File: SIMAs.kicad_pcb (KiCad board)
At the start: 2 copper layers, 67.5 x 75.5 mm, 89 parts, among them J1 USB_C_Receptacle_PowerOnly_6P, J10 Conn_01x02_Pin, J11 Conn_01x03_Pin, J12 Conn_01x03_Pin, J13 Conn_01x05_Pin, J14 Conn_01x02_Pin, J2 Conn_01x02_Socket, J3 Conn_01x04_Socket, J4 Conn_01x04_Socket, J5 Conn_01x04_Socket, J6 Conn_01x03_Socket, J7 Bateria, J8 Conn_01x02_Socket, J9 Conn_01x03_Socket, Q1 QM6015D, U1 mini_esp32, U2 BQ25628ERYKR, U3 TPS611781RNWR, U4 TLV61070ADBV, U8 DRV8876PWPR, U9 DRV8876PWPR

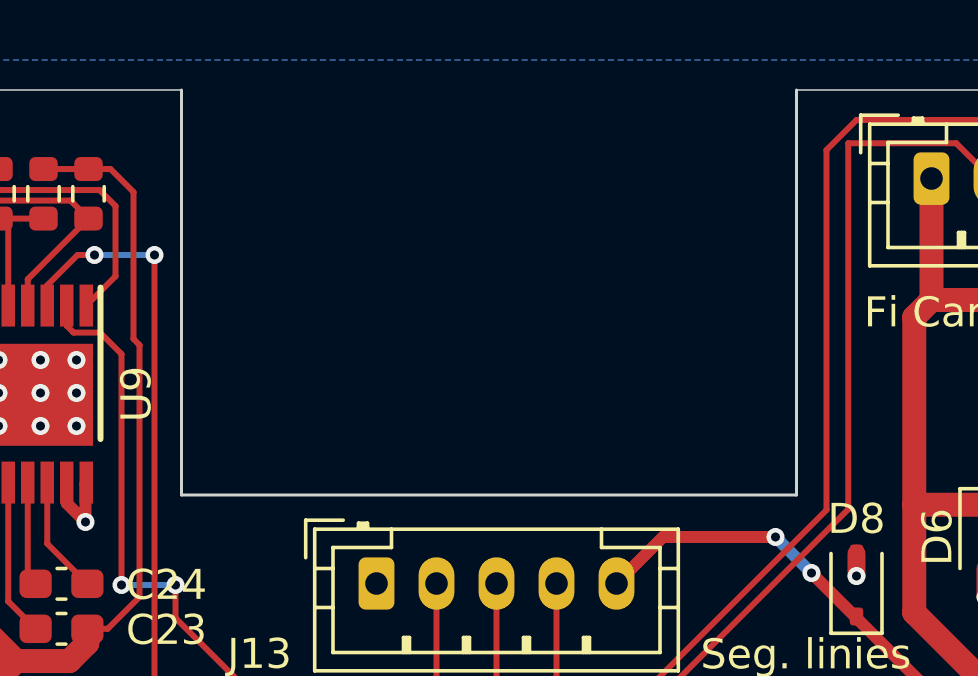
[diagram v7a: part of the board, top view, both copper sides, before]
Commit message: Afegit avellanat i teardrops
S'ha afegit avellanat en la cantonada interna de la placa per permetre la fabricació, i s'han afegit les llàgrimes a les pistes.
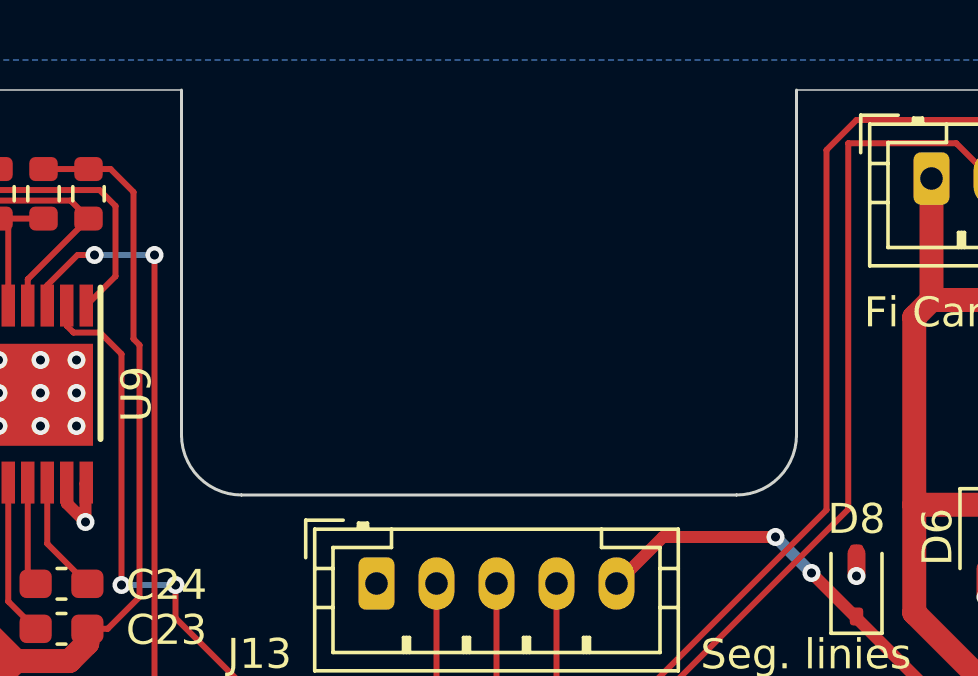
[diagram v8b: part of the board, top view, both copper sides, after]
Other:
- outline, holes or cut-outs redrawn
